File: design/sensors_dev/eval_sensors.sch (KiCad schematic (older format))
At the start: 33 parts, among them J4 Conn_01x12, U2 BMC150, U3 LSM6DS3HTR, U4 BMG250, U5 MS5607-02BA03, U6 LIS3DHTR

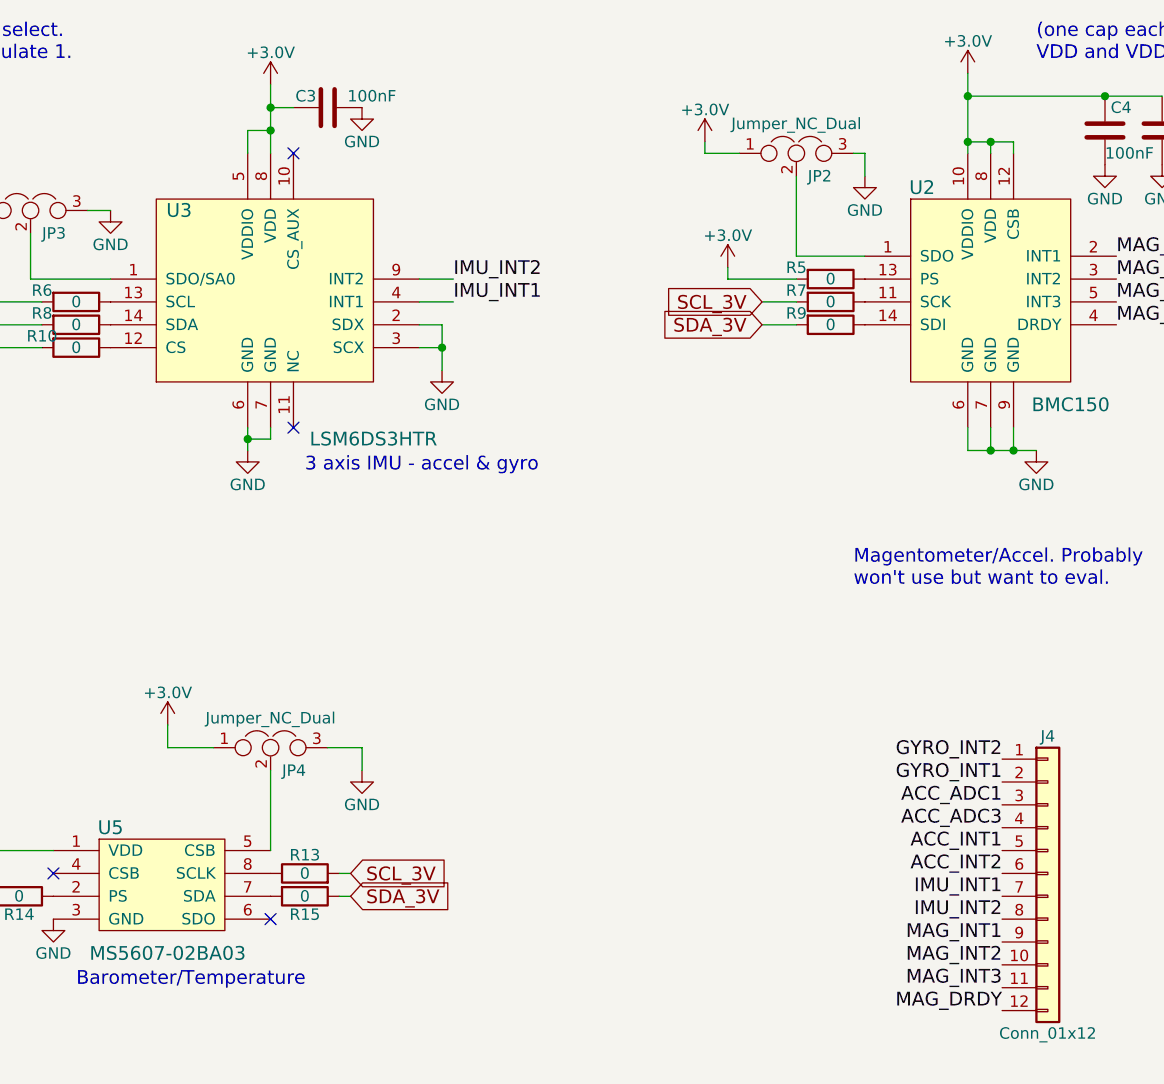
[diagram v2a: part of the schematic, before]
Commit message: Redo board placement and routing
Will send to fab after final review.
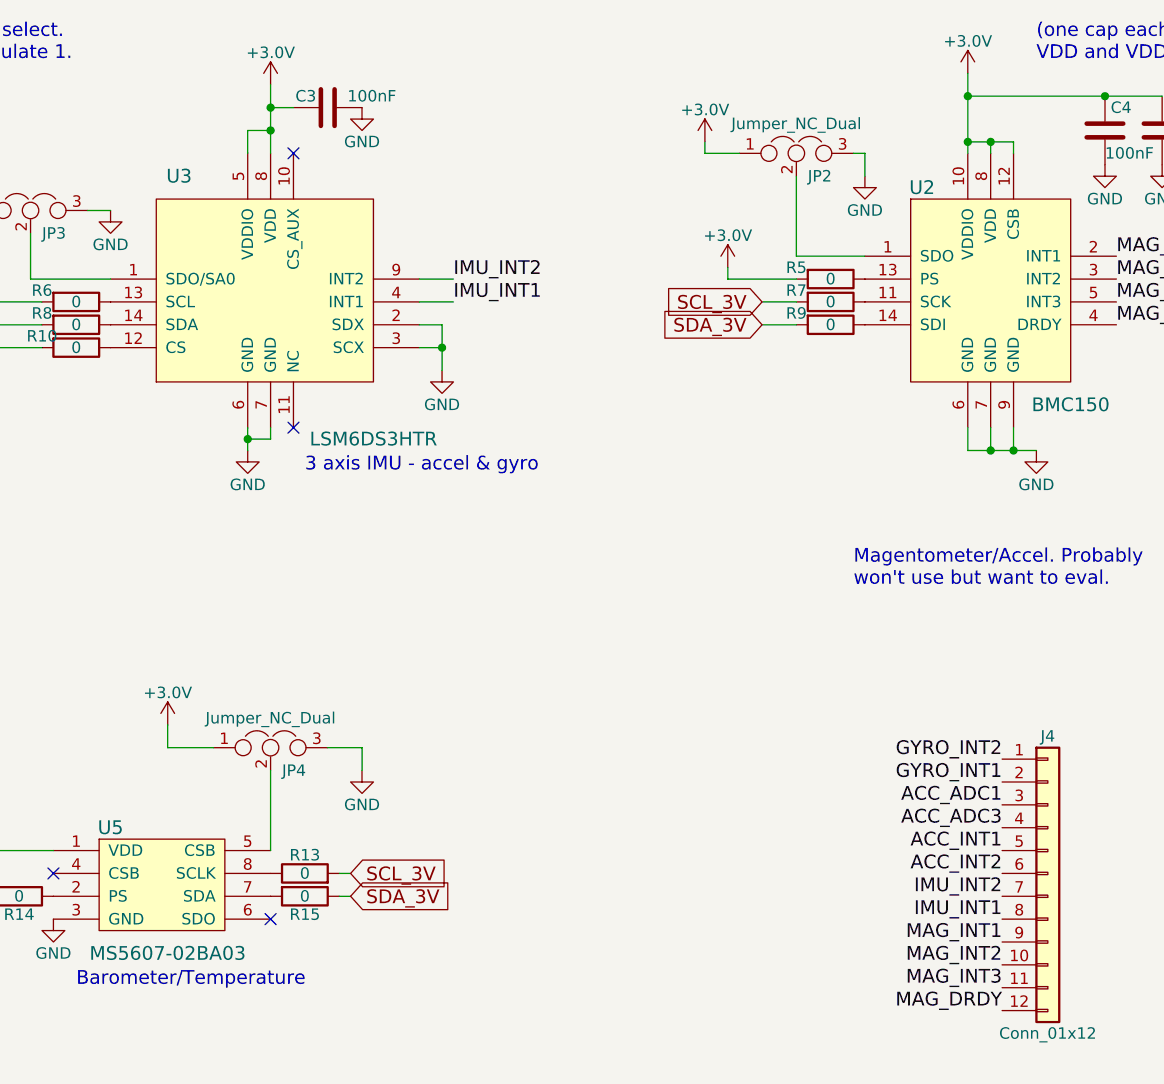
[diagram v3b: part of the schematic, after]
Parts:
- C3, C4, C5, C6, C8, C9, R11, R12, R19: footprint Capacitors_SMD:C_0805_HandSoldering -> Capacitors_SMD:C_0603_HandSoldering
- R10, R13, R14, R15, R16, R17, R18, R5, R6, R7, R8, R9: footprint Resistors_SMD:R_0805_HandSoldering -> Resistors_SMD:R_0603_HandSoldering
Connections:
- net IMU_INT1: now also J4.8 (Pin_8); no longer J4.7 (Pin_7)
- net IMU_INT2: now also J4.7 (Pin_7); no longer J4.8 (Pin_8)
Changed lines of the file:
@@
 U 1 1 5AAC81C6
 P 6550 2650
-F 0 "U3" H 6150 3100 60  0000 C CNN
+F 0 "U3" H 6150 3250 60  0000 C CNN
 F 1 "LSM6DS3HTR" H 7000 2100 60  0000 C CNN
 F 2 "LSM6DS3:PQFN50P300X250X86-14N" H 6450 2400 60  0001 C CNN
@@
 F 0 "C3" V 6850 1800 50  0000 L CNN
 F 1 "100nF" V 6850 1450 50  0000 L CNN
-F 2 "Capacitors_SMD:C_0805_HandSoldering" H 6838 1600 50  0001 C CNN
+F 2 "Capacitors_SMD:C_0603_HandSoldering" H 6838 1600 50  0001 C CNN
 F 3 "" H 6800 1750 50  0001 C CNN
 	1    6800 1750
@@
 F 0 "R6" V 5650 2450 50  0000 C CNN
 F 1 "0" V 5700 2600 50  0000 C CNN
-F 2 "Resistors_SMD:R_0805_HandSoldering" V 5630 2600 50  0001 C CNN
+F 2 "Resistors_SMD:R_0603_HandSoldering" V 5630 2600 50  0001 C CNN
 F 3 "" H 5700 2600 50  0001 C CNN
 	1    5700 2600
@@
 F 0 "R8" V 5650 2550 50  0000 C CNN
 F 1 "0" V 5700 2700 50  0000 C CNN
-F 2 "Resistors_SMD:R_0805_HandSoldering" V 5630 2700 50  0001 C CNN
+F 2 "Resistors_SMD:R_0603_HandSoldering" V 5630 2700 50  0001 C CNN
 F 3 "" H 5700 2700 50  0001 C CNN
 	1    5700 2700
@@
 F 0 "C9" H 5100 5450 50  0000 L CNN
 F 1 "100nF" H 4950 5250 50  0000 L CNN
-F 2 "Capacitors_SMD:C_0805_HandSoldering" H 5238 5200 50  0001 C CNN
+F 2 "Capacitors_SMD:C_0603_HandSoldering" H 5238 5200 50  0001 C CNN
 F 3 "" H 5200 5350 50  0001 C CNN
 	1    5200 5350
@@
 F 0 "R13" V 6780 5100 50  0000 C CNN
 F 1 "0" V 6700 5100 50  0000 C CNN
-F 2 "Resistors_SMD:R_0805_HandSoldering" V 6630 5100 50  0001 C CNN
+F 2 "Resistors_SMD:R_0603_HandSoldering" V 6630 5100 50  0001 C CNN
 F 3 "" H 6700 5100 50  0001 C CNN
 	1    6700 5100
@@
 F 0 "R15" V 6780 5200 50  0000 C CNN
 F 1 "0" V 6700 5200 50  0000 C CNN
-F 2 "Resistors_SMD:R_0805_HandSoldering" V 6630 5200 50  0001 C CNN
+F 2 "Resistors_SMD:R_0603_HandSoldering" V 6630 5200 50  0001 C CNN
 F 3 "" H 6700 5200 50  0001 C CNN
 	1    6700 5200
@@
 F 0 "R7" V 8950 2450 50  0000 C CNN
 F 1 "0" V 9000 2600 50  0000 C CNN
-F 2 "Resistors_SMD:R_0805_HandSoldering" V 8930 2600 50  0001 C CNN
+F 2 "Resistors_SMD:R_0603_HandSoldering" V 8930 2600 50  0001 C CNN
 F 3 "" H 9000 2600 50  0001 C CNN
 	1    9000 2600
@@
 F 0 "R9" V 8950 2550 50  0000 C CNN
 F 1 "0" V 9000 2700 50  0000 C CNN
-F 2 "Resistors_SMD:R_0805_HandSoldering" V 8930 2700 50  0001 C CNN
+F 2 "Resistors_SMD:R_0603_HandSoldering" V 8930 2700 50  0001 C CNN
 F 3 "" H 9000 2700 50  0001 C CNN
 	1    9000 2700
@@
 F 0 "C4" H 10225 1950 50  0000 L CNN
 F 1 "100nF" H 10200 1750 50  0000 L CNN
-F 2 "Capacitors_SMD:C_0805_HandSoldering" H 10238 1700 50  0001 C CNN
+F 2 "Capacitors_SMD:C_0603_HandSoldering" H 10238 1700 50  0001 C CNN
 F 3 "" H 10200 1850 50  0001 C CNN
 	1    10200 1850
@@
 F 0 "C5" H 10475 1950 50  0000 L CNN
 F 1 "100nF" H 10475 1750 50  0000 L CNN
-F 2 "Capacitors_SMD:C_0805_HandSoldering" H 10488 1700 50  0001 C CNN
+F 2 "Capacitors_SMD:C_0603_HandSoldering" H 10488 1700 50  0001 C CNN
 F 3 "" H 10450 1850 50  0001 C CNN
 	1    10450 1850
@@
 F 0 "R5" V 8950 2350 50  0000 C CNN
 F 1 "0" V 9000 2500 50  0000 C CNN
-F 2 "Resistors_SMD:R_0805_HandSoldering" V 8930 2500 50  0001 C CNN
+F 2 "Resistors_SMD:R_0603_HandSoldering" V 8930 2500 50  0001 C CNN
 F 3 "" H 9000 2500 50  0001 C CNN
 	1    9000 2500
@@
 F 0 "R10" V 5650 2650 50  0000 C CNN
 F 1 "0" V 5700 2800 50  0000 C CNN
-F 2 "Resistors_SMD:R_0805_HandSoldering" V 5630 2800 50  0001 C CNN
+F 2 "Resistors_SMD:R_0603_HandSoldering" V 5630 2800 50  0001 C CNN
 F 3 "" H 5700 2800 50  0001 C CNN
 	1    5700 2800
@@
 F 0 "R14" V 5530 5200 50  0000 C CNN
 F 1 "0" V 5450 5200 50  0000 C CNN
-F 2 "Resistors_SMD:R_0805_HandSoldering" V 5380 5200 50  0001 C CNN
+F 2 "Resistors_SMD:R_0603_HandSoldering" V 5380 5200 50  0001 C CNN
 F 3 "" H 5450 5200 50  0001 C CNN
 	1    5450 5200
@@
 F 0 "R16" V 2200 5850 50  0000 C CNN
 F 1 "0" V 2250 6000 50  0000 C CNN
-F 2 "Resistors_SMD:R_0805_HandSoldering" V 2180 6000 50  0001 C CNN
+F 2 "Resistors_SMD:R_0603_HandSoldering" V 2180 6000 50  0001 C CNN
 F 3 "" H 2250 6000 50  0001 C CNN
 	1    2250 6000
@@
 F 0 "R17" V 2200 5950 50  0000 C CNN
 F 1 "0" V 2250 6100 50  0000 C CNN
-F 2 "Resistors_SMD:R_0805_HandSoldering" V 2180 6100 50  0001 C CNN
+F 2 "Resistors_SMD:R_0603_HandSoldering" V 2180 6100 50  0001 C CNN
 F 3 "" H 2250 6100 50  0001 C CNN
 	1    2250 6100
@@
 F 0 "R18" V 2200 6050 50  0000 C CNN
 F 1 "0" V 2250 6200 50  0000 C CNN
-F 2 "Resistors_SMD:R_0805_HandSoldering" V 2180 6200 50  0001 C CNN
+F 2 "Resistors_SMD:R_0603_HandSoldering" V 2180 6200 50  0001 C CNN
 F 3 "" H 2250 6200 50  0001 C CNN
 	1    2250 6200
@@
 F 0 "C8" H 3825 5350 50  0000 L CNN
 F 1 "100nF" H 3825 5150 50  0000 L CNN
-F 2 "Capacitors_SMD:C_0805_HandSoldering" H 3838 5100 50  0001 C CNN
+F 2 "Capacitors_SMD:C_0603_HandSoldering" H 3838 5100 50  0001 C CNN
 F 3 "" H 3800 5250 50  0001 C CNN
 	1    3800 5250
@@
 Text Label 9750 5100 2    60   ~ 0
 ACC_INT2
+Text Label 9750 5300 2    60   ~ 0
+IMU_INT1
 Text Label 9750 5200 2    60   ~ 0
-IMU_INT1
-Text Label 9750 5300 2    60   ~ 0
 IMU_INT2
 Text Label 9750 5400 2    60   ~ 0
@@
 F 0 "C6" H 3275 1950 50  0000 L CNN
 F 1 "100nF" H 3275 1750 50  0000 L CNN
-F 2 "Capacitors_SMD:C_0805_HandSoldering" H 3288 1700 50  0001 C CNN
+F 2 "Capacitors_SMD:C_0603_HandSoldering" H 3288 1700 50  0001 C CNN
 F 3 "" H 3250 1850 50  0001 C CNN
 	1    3250 1850
@@
 F 0 "R12" V 2000 2350 50  0000 C CNN
 F 1 "0" V 2050 2550 50  0000 C CNN
-F 2 "Capacitors_SMD:C_0805_HandSoldering" V 1980 2550 50  0001 C CNN
+F 2 "Capacitors_SMD:C_0603_HandSoldering" V 1980 2550 50  0001 C CNN
 F 3 "" H 2050 2550 50  0001 C CNN
 	1    2050 2550
@@
 F 0 "R19" V 2000 2450 50  0000 C CNN
 F 1 "0" V 2050 2650 50  0000 C CNN
-F 2 "Capacitors_SMD:C_0805_HandSoldering" V 1980 2650 50  0001 C CNN
+F 2 "Capacitors_SMD:C_0603_HandSoldering" V 1980 2650 50  0001 C CNN
 F 3 "" H 2050 2650 50  0001 C CNN
 	1    2050 2650
@@
 F 0 "R11" V 2280 2050 50  0000 C CNN
 F 1 "0" V 2200 2050 50  0000 C CNN
-F 2 "Capacitors_SMD:C_0805_HandSoldering" V 2130 2050 50  0001 C CNN
+F 2 "Capacitors_SMD:C_0603_HandSoldering" V 2130 2050 50  0001 C CNN
 F 3 "" H 2200 2050 50  0001 C CNN
 	1    2200 2050
